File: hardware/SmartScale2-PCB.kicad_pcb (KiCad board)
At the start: 4 copper layers, 40 x 50 mm, 57 parts, among them J1 Conn_ARM_JTAG_SWD_10, J2 USB_C_Receptacle_USB2.0_16P, J3 Conn_01x02, J4 Conn_01x04, J5 Conn_01x03_MountingPin, J6 Conn_01x04_MountingPin, Q1 MMBT4403, SW1 SW_Push_JTP-1130, U1 ESP32-C6-WROOM-1, U2 MCP73831-2-OT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

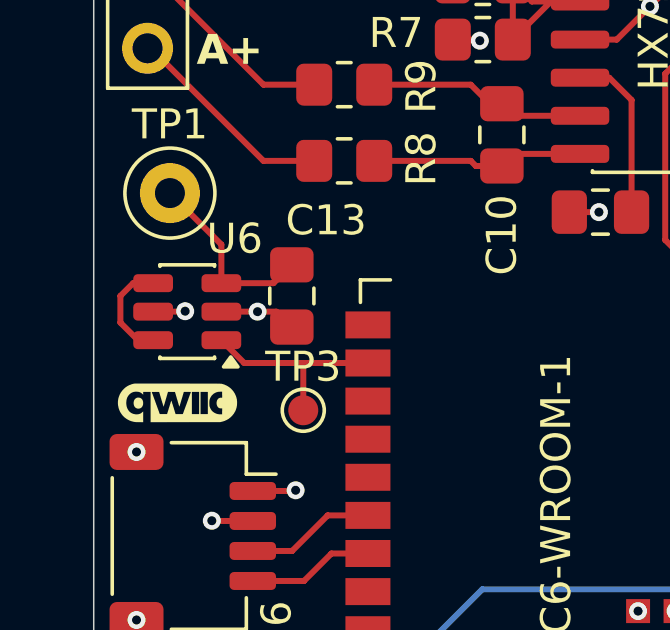
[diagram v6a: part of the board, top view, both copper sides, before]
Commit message: Add jumpers for touch ic pins, render ui on display
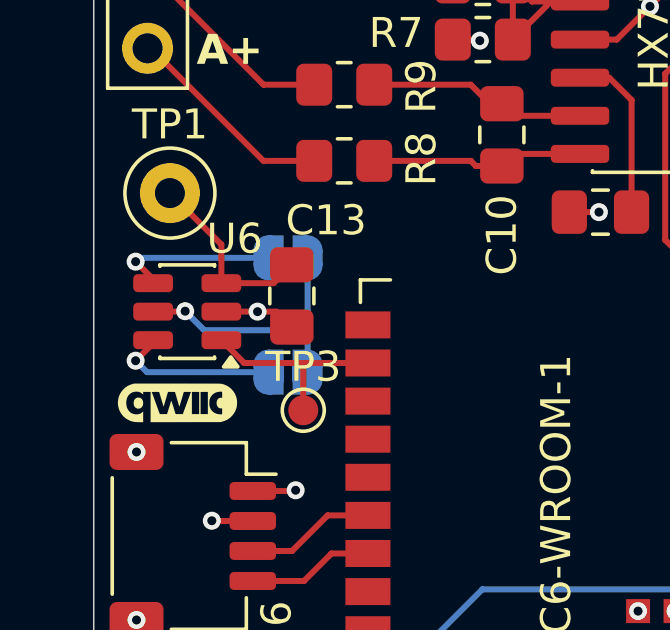
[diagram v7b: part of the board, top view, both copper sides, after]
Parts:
- added JP6: Jumper_2_Small_Open, Jumper:SolderJumper-2_P1.3mm_Open_RoundedPad1.0x1.5mm, B.Cu at (42.9, 66.6)
- added JP7: Jumper_2_Small_Open, Jumper:SolderJumper-2_P1.3mm_Open_RoundedPad1.0x1.5mm, B.Cu at (42.9, 70.4)
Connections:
- U6 pad 4: Net-(U6-AHLB) -> Net-(JP6-A)
- U6 pad 6: Net-(U6-AHLB) -> Net-(JP7-A)
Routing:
- net +3V3: track 32.8 -> 41.2 mm
- net Net-(JP7-A): track 0.00 -> 5.51 mm, vias 0 -> 1
- net Net-(JP6-A): track 0.00 -> 5.44 mm, vias 0 -> 1
- net Net-(U6-AHLB): track 3.49 -> 0.00 mm

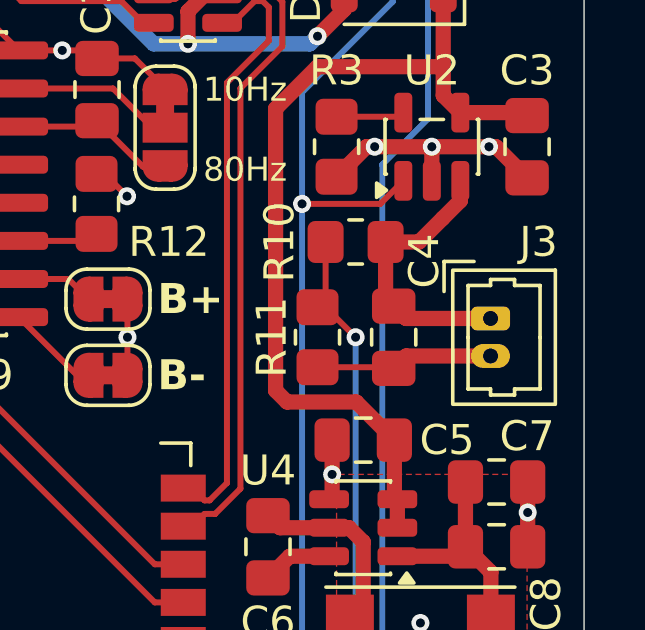
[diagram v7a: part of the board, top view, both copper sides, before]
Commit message: Add battery connector labels
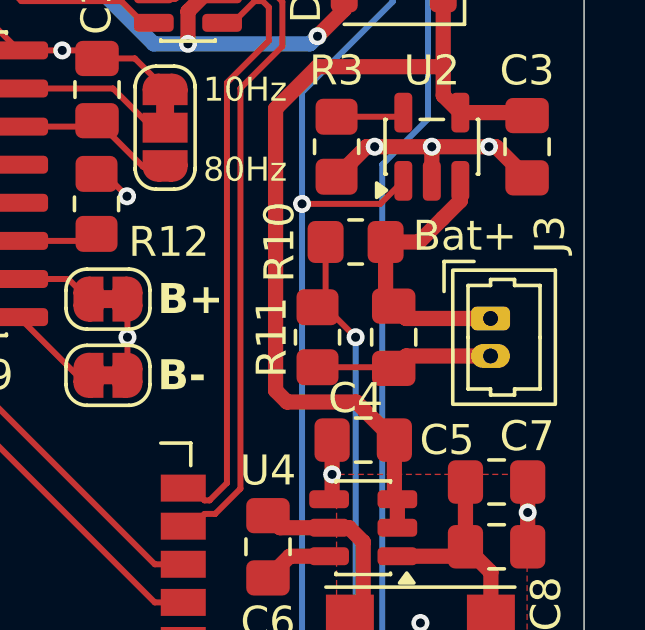
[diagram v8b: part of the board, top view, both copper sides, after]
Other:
- board text added: "+"
- board text added: "Bat+"
- board text added: "GND"
- board text added: "Single Cell LiPo Molex PicoBlade"
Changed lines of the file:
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@@
 		(tags "capacitor handsolder")
 		(property "Reference" "C4"
-			(at -2.54 -1.016 270)
+			(at 2.032 1.27 180)
 			(layer "F.SilkS")
 			(effects
@@
 		(tags "connector Molex PicoBlade vertical")
 		(property "Reference" "J3"
-			(at -2.55 -1.598 0)
+			(at -2.804 -1.979 90)
 			(layer "F.SilkS")
 			(effects
@@
 		)
 	)
+	(gr_text "Bat+"
+		(at 70.755 60.996 0)
+		(layer "F.SilkS")
+		(effects
+			(font
+				(size 1 1)
+				(thickness 0.1)
+			)
+			(justify left bottom)
+		)
+	)
 	(gr_text "USB-C"
 		(at 56.465 45 0)
@@
 		)
 	)
+	(gr_text "Single Cell LiPo\nMolex PicoBlade"
+		(at 72.152 57.567 90)
+		(layer "B.SilkS")
+		(effects
+			(font
+				(size 1 1)
+				(thickness 0.1)
+			)
+			(justify left bottom mirror)
+		)
+	)
+	(gr_text "GND"
+		(at 73.295 67.092 90)
+		(layer "B.SilkS" knockout)
+		(effects
+			(font
+				(size 1 1)
+				(thickness 0.25)
+				(bold yes)
+			)
+			(justify mirror)
+		)
+	)
+	(gr_text "+"
+		(at 73.295 60.996 0)
+		(layer "B.SilkS")
+		(effects
+			(font
+				(size 2 2)
+				(thickness 0.3)
+				(bold yes)
+			)
+			(justify mirror)
+		)
+	)
